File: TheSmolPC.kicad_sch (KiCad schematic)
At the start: 0 parts

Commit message: partially finished the schematic ig
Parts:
- added C1, C12, C2: 0.1u, Capacitor_SMD:C_0402_1005Metric, symbol Device:C
- added C10, C11, C16, C17, C18, C19, C20, C21, C22, C23, C24, C8, C9: 100n, Capacitor_SMD:C_0402_1005Metric, symbol Device:C
- added C13, C14, C15: 10u, Capacitor_SMD:C_0402_1005Metric, symbol Device:C
- added C3, C4: 34pF, Capacitor_SMD:C_0402_1005Metric, symbol Device:C
- added C5, C6, C7: 4.7u, Capacitor_SMD:C_0402_1005Metric, symbol Device:C
- added D1: MBR120VLSFT1G, Diode_SMD:D_SOD-123F, symbol Device:D_Schottky
- added J1: USB_C_Receptacle_USB2.0_16P, Connector_USB:USB_C_Receptacle_GCT_USB4105-xx-A_16P_TopMnt_Horizontal, symbol Connector:USB_C_Receptacle_USB2.0_16P
- added J2, J3: USB_A, Connector_USB:USB_A_Receptacle_GCT_USB1046, symbol Connector:USB_A
- added J4: HDMI_A, Connector_Video:HDMI_A_Molex_208658-1001_Horizontal, symbol Connector:HDMI_A
- added L1: 2.2u, Inductor_SMD:L_Changjiang_FNR3015S, symbol Device:L
- added L2: 3.3u, Inductor_SMD:L_Murata_DFE201610P, symbol Device:L
- added R1, R2: 5.1k, Resistor_SMD:R_0402_1005Metric, symbol Device:R
- added R3, R4: 27, Resistor_SMD:R_0402_1005Metric, symbol Device:R
- added R5: 100, Resistor_SMD:R_0402_1005Metric, symbol Device:R
- added R5: 560k, Resistor_SMD:R_0402_1005Metric, symbol Device:R
- added R6: 100k, Resistor_SMD:R_0402_1005Metric, symbol Device:R
- added R7: 33, Resistor_SMD:R_0402_1005Metric, symbol Device:R
- added R8: 10k, Resistor_SMD:R_0402_1005Metric, symbol Device:R
- added RN1, RN2, RN3, RN4: 220, Resistor_SMD:R_Array_Convex_2x0402, symbol Device:R_Pack02
- added U1: RP2350B-QFN80, Package_DFN_QFN:QFN-80-1EP_10x10mm_P0.4mm_EP3.4x3.4mm_ThermalVias, symbol rp2350b-qfn80:RP2350B-QFN80
- added U2: CH334R, Package_QFP:HTQFP-64-1EP_10x10mm_P0.5mm_EP8x8mm_Mask4.4x4.4mm_ThermalVias, symbol Interface_USB:CH334R
- added U3: TPS63000, Package_SON:Texas_DRC0010J_ThermalVias, symbol Regulator_Switching:TPS63000
- added U4: W25Q128JVS, Package_SO:SOIC-8_5.3x5.3mm_P1.27mm, symbol Memory_Flash:W25Q128JVS
- added U5: APS6404L-SQRx-SN, Package_SO:SOIC-8_3.9x4.9mm_P1.27mm, symbol Memory_RAM:APS6404L-SQRx-SN
- added Y1: 12MHz, Crystal:Crystal_SMD_Abracon_ABM3-2Pin_5.0x3.2mm, symbol Device:Crystal_Small
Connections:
- new net: C4.1, U2.15 (XO), Y1.1
- new net: C3.1, U2.16 (XI), Y1.2
- new net: C7.1, R7.2, U1.61 (VREG_AVDD)
- new net: R4.1, U1.66 (USB_DM)
- new net: R3.1, U1.67 (USB_DP)
- new net: C12.1, R5.2, U3.6 (EN), U3.7 (PS/SYNC), U3.8 (VINA)
- new net: R5.2, R6.1, U3.10 (FB)
- new net: L1.1, U3.2 (L2)
- new net: L1.2, U3.4 (L1)
- new net: J1.A5 (CC1), R1.1
- new net: J1.B5 (CC2), R2.1
- new net +1V1: C21.1, C22.1, C23.1, C5.1, L2.1, U1.10 (DVDD), U1.32 (DVDD), U1.51 (DVDD), U1.65 (VREG_FB), U1.69 (QSPI_IOVDD)
- new net +3V3: C10.1, C11.1, C14.1, C15.1, C16.1, C17.1, C18.1, C19.1, C20.1, C24.1, C6.1, C8.1, C9.1, R5.1, R7.1, R8.1, U1.15 (IOVDD), U1.24 (IOVDD), U1.29 (IOVDD), U1.41 (IOVDD), U1.5 (IOVDD), U1.50 (IOVDD), U1.59 (ADC_AVDD), U1.60 (IOVDD), U1.64 (VREG_VIN), U1.68 (USB_OTP_VDD), U1.76 (IOVDD), U3.1 (VOUT), U4.8 (VCC)
- new net +3V3_USB: C1.1, U2.13 (VDD33)
- new net DVI_CK+: J4.10 (CK+), RN4.4 (R1.2)
- new net DVI_CK-: J4.12 (CK-), RN4.3 (R2.2)
- new net DVI_D0+: J4.7 (D0+), RN3.4 (R1.2)
- new net DVI_D0-: J4.9 (D0-), RN3.3 (R2.2)
- new net DVI_D1+: J4.4 (D1+), RN2.4 (R1.2)
- new net DVI_D1-: J4.6 (D1-), RN2.3 (R2.2)
- new net DVI_D2+: J4.1 (D2+), RN1.4 (R1.2)
- new net DVI_D2-: J4.3 (D2-), RN1.3 (R2.2)
- new net FLASH_CLK: U1.71 (QSPI_SCLK), U4.6 (CLK), U5.6 (SCLK)
- new net FLASH_CS: R8.2, U1.75 (QSPI_SS), U4.1 (~{CS})
- new net FLASH_SD0: U1.72 (QSPI_SD0), U4.5 (DI/IO_{0}), U5.5 (SI/SIO0)
- new net FLASH_SD1: U1.74 (QSPI_SD1), U4.2 (DO/IO_{1}), U5.2 (SO/SIO1)
- new net FLASH_SD2: U1.73 (QSPI_SD2), U4.3 (~{WP}/IO_{2}), U5.3 (SIO2)
- new net FLASH_SD3: U1.70 (QSPI_SD3), U4.7 (~{HOLD}/~{RESET}/IO_{3}), U5.7 (SIO3)
- new net GND: C1.2, C10.2, C11.2, C12.2, C13.2, C14.2, C15.2, C16.2, C17.2, C18.2, C19.2, C2.2, C20.2, C21.2, C22.2, C23.2, C24.2, C3.2, C4.2, C5.2, C6.2, C7.2, C8.2, C9.2, J1.A1 (GND), J1.A12 (GND), J1.B1 (GND), J1.B12 (GND), J1.S1 (SHIELD), J2.4 (GND), J2.5 (Shield), J3.4 (GND), J3.5 (Shield), R1.2, R2.2, R6.2, U1.62 (VREG_PGND), U2.14 (GND), U3.11 (PGND), U3.3 (PGND), U3.9 (GND), U4.4 (GND)
- new net HSTX_CK+: RN4.1 (R1.1), U1.11 (GPIO12)
- new net HSTX_CK-: RN4.2 (R2.1), U1.12 (GPIO13)
- new net HSTX_D0+: RN3.1 (R1.1), U1.13 (GPIO14)
- new net HSTX_D0-: RN3.2 (R2.1), U1.14 (GPIO15)
- new net HSTX_D1+: RN2.1 (R1.1), U1.16 (GPIO16)
- new net HSTX_D1-: RN2.2 (R2.1), U1.17 (GPIO17)
- new net HSTX_D2+: RN1.1 (R1.1), U1.18 (GPIO18)
- new net HSTX_D2-: RN1.2 (R2.1), U1.19 (GPIO19)
- new net USB0_D+: J2.3 (D+), U2.8 (DP1+)
- new net USB0_D-: J2.2 (D-), U2.7 (DM1-)
- new net USB1_D+: J3.3 (D+), U2.6 (DP2+)
- new net USB1_D-: J3.2 (D-), U2.5 (DM2-)
- new net USB_D+: J1.A6 (D+), J1.B6 (D+), R3.2, U2.11 (DPU+)
- new net USB_D-: J1.A7 (D-), J1.B7 (D-), R4.2, U2.10 (DMU-)
- new net VBUS: D1.2 (A), J1.A4 (VBUS), J1.A9 (VBUS), J1.B4 (VBUS), J1.B9 (VBUS), J2.1 (VBUS), J3.1 (VBUS)
- new net VREG_LX: L2.2, U1.63 (VREG_LX)
- new net VSYS: C13.1, C2.1, D1.1 (K), R5.1, U2.12 (V5), U3.5 (VIN)
- no-connect marks 0 -> 8
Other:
- note added: "I'll probably use this USB line as usages for USB by the host PC or the RP2350"
- note added: "who needs CEC anw"

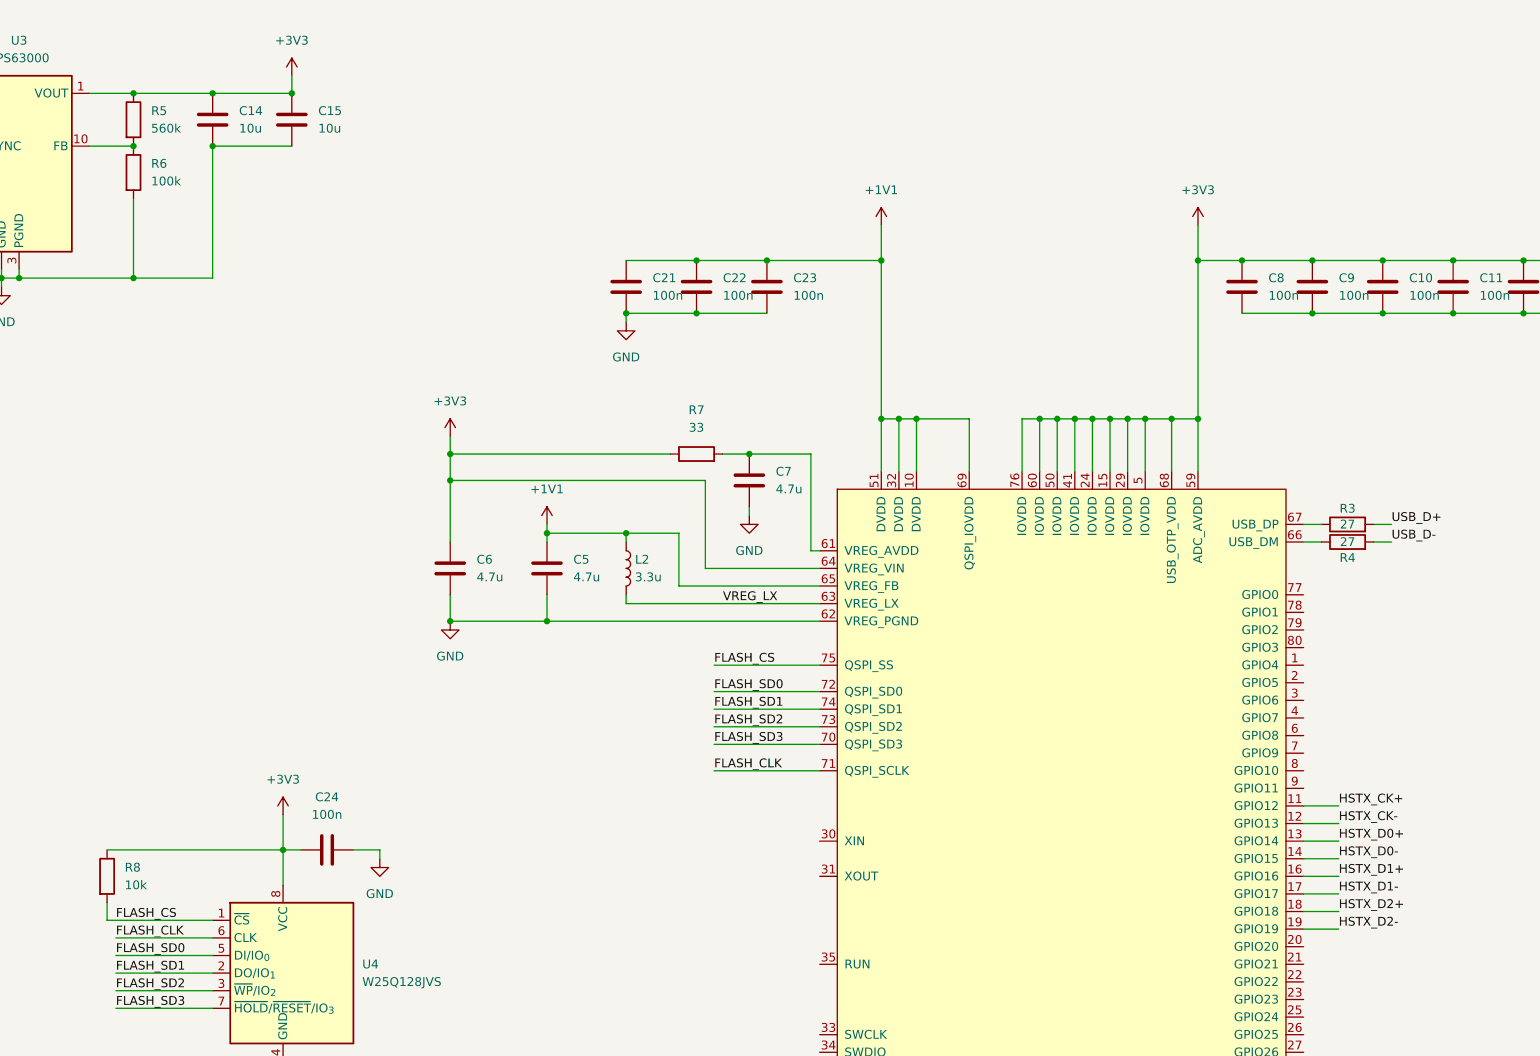
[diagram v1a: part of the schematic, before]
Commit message: fixed the schematic differential pair polarities (tested with the pcb editor)
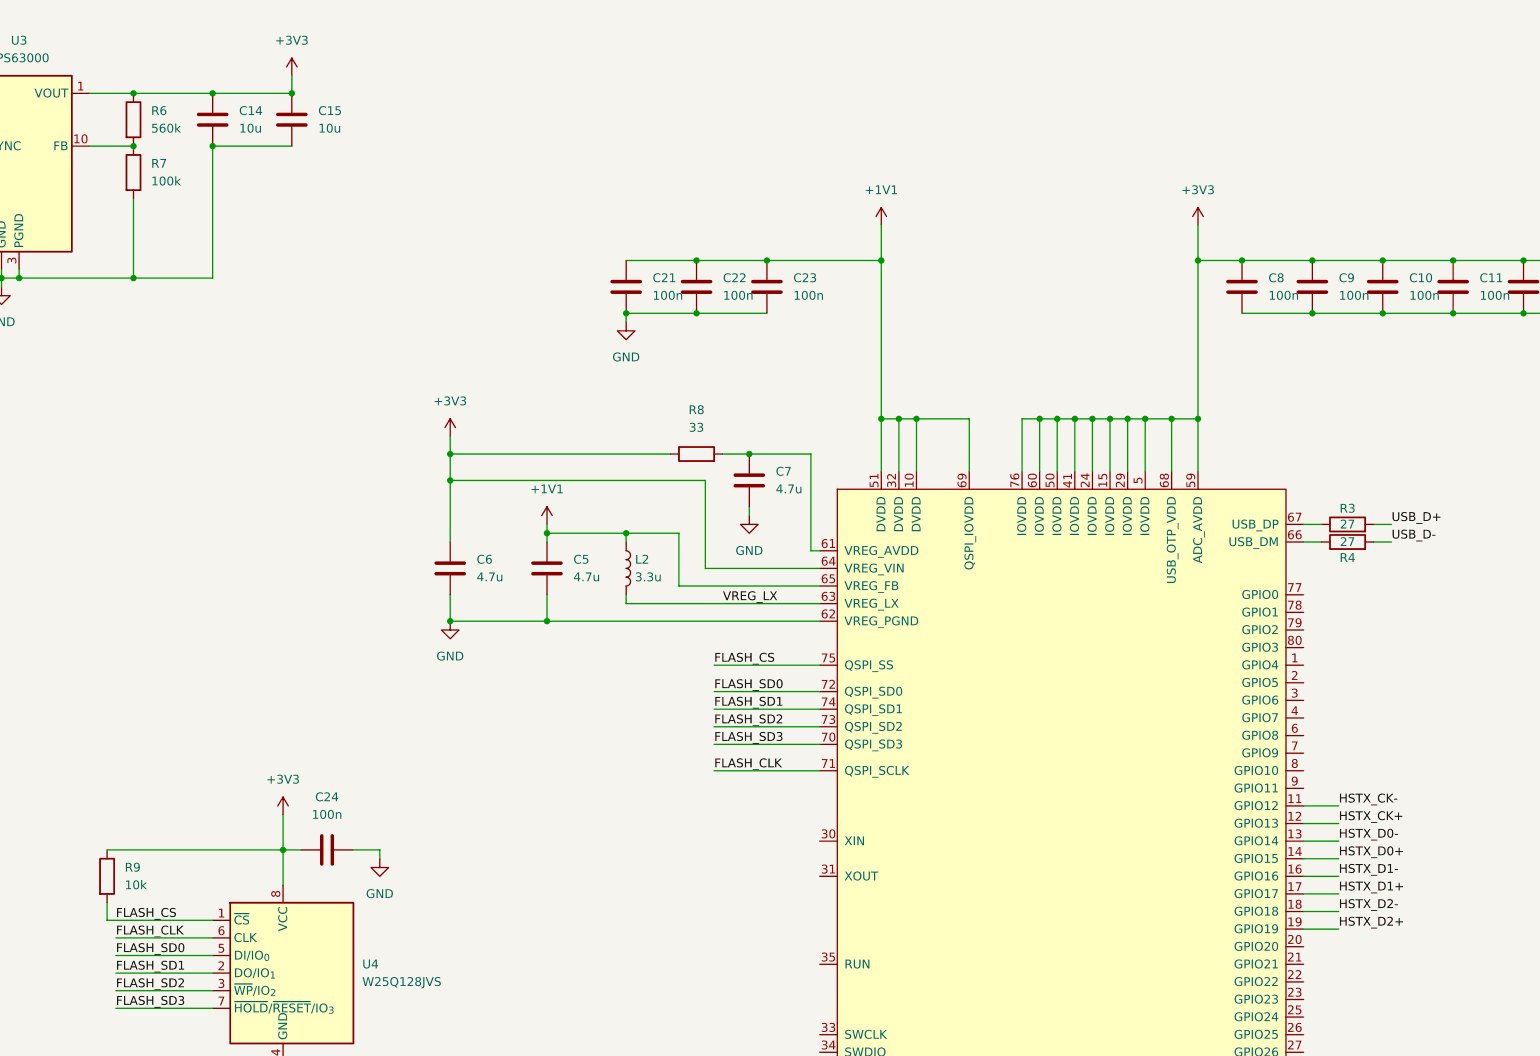
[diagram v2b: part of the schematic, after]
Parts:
- U2: footprint Package_QFP:HTQFP-64-1EP_10x10mm_P0.5mm_EP8x8mm_Mask4.4x4.4mm_ThermalVias -> Package_SO:QSOP-16_3.9x4.9mm_P0.635mm
- renumbered R5 to R6, R6 to R7, R7 to R8, R8 to R9
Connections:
- net HSTX_CK+: now also U1.12 (GPIO13); no longer U1.11 (GPIO12)
- net HSTX_CK-: now also U1.11 (GPIO12); no longer U1.12 (GPIO13)
- net HSTX_D0+: now also U1.14 (GPIO15); no longer U1.13 (GPIO14)
- net HSTX_D0-: now also U1.13 (GPIO14); no longer U1.14 (GPIO15)
- net HSTX_D1+: now also U1.17 (GPIO17); no longer U1.16 (GPIO16)
- net HSTX_D1-: now also U1.16 (GPIO16); no longer U1.17 (GPIO17)
- net HSTX_D2+: now also U1.19 (GPIO19); no longer U1.18 (GPIO18)
- net HSTX_D2-: now also U1.18 (GPIO18); no longer U1.19 (GPIO19)
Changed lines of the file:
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@@
 	(wire
 		(pts
-			(xy 322.58 132.08) (xy 317.5 132.08)
-		)
-		(stroke
-			(width 0)
-			(type default)
-		)
-	)
-	(wire
-		(pts
 			(xy 146.05 153.67) (xy 160.02 153.67)
 		)
@@
 	(wire
 		(pts
-			(xy 322.58 129.54) (xy 317.5 129.54)
-		)
-		(stroke
-			(width 0)
-			(type default)
-		)
-	)
-	(wire
-		(pts
 			(xy 45.72 113.03) (xy 35.56 113.03)
 		)
@@
 	(wire
 		(pts
-			(xy 82.55 111.76) (xy 69.85 111.76)
+			(xy 322.58 142.24) (xy 317.5 142.24)
 		)
 		(stroke
@@
 	(wire
 		(pts
-			(xy 146.05 158.75) (xy 160.02 158.75)
+			(xy 317.5 129.54) (xy 322.58 129.54)
 		)
 		(stroke
@@
 	(wire
 		(pts
-			(xy 302.26 73.66) (xy 302.26 81.28)
+			(xy 82.55 111.76) (xy 69.85 111.76)
 		)
 		(stroke
@@
 	(wire
 		(pts
-			(xy 292.1 73.66) (xy 294.64 73.66)
+			(xy 146.05 158.75) (xy 160.02 158.75)
 		)
 		(stroke
@@
 	(wire
 		(pts
-			(xy 322.58 142.24) (xy 317.5 142.24)
+			(xy 302.26 73.66) (xy 302.26 81.28)
+		)
+		(stroke
+			(width 0)
+			(type default)
+		)
+	)
+	(wire
+		(pts
+			(xy 292.1 73.66) (xy 294.64 73.66)
 		)
 		(stroke
@@
 	(wire
 		(pts
-			(xy 322.58 139.7) (xy 317.5 139.7)
+			(xy 232.41 118.11) (xy 247.65 118.11)
 		)
 		(stroke
@@
 	(wire
 		(pts
-			(xy 232.41 118.11) (xy 247.65 118.11)
+			(xy 322.58 144.78) (xy 317.5 144.78)
 		)
 		(stroke
@@
 	(wire
 		(pts
-			(xy 322.58 134.62) (xy 317.5 134.62)
-		)
-		(stroke
-			(width 0)
-			(type default)
-		)
-	)
-	(wire
-		(pts
 			(xy 287.02 73.66) (xy 287.02 81.28)
 		)
@@
 	(wire
 		(pts
+			(xy 322.58 134.62) (xy 317.5 134.62)
+		)
+		(stroke
+			(width 0)
+			(type default)
+		)
+	)
+	(wire
+		(pts
 			(xy 59.69 67.31) (xy 59.69 81.28)
 		)
@@
 	(wire
 		(pts
+			(xy 322.58 147.32) (xy 317.5 147.32)
+		)
+		(stroke
+			(width 0)
+			(type default)
+		)
+	)
+	(wire
+		(pts
 			(xy 289.56 73.66) (xy 292.1 73.66)
 		)
@@
 	(wire
 		(pts
+			(xy 322.58 139.7) (xy 317.5 139.7)
+		)
+		(stroke
+			(width 0)
+			(type default)
+		)
+	)
+	(wire
+		(pts
 			(xy 208.28 102.87) (xy 247.65 102.87)
 		)
@@
 	(wire
 		(pts
+			(xy 322.58 132.08) (xy 317.5 132.08)
+		)
+		(stroke
+			(width 0)
+			(type default)
+		)
+	)
+	(wire
+		(pts
 			(xy 85.09 92.71) (xy 85.09 102.87)
 		)
@@
 	(wire
 		(pts
-			(xy 322.58 147.32) (xy 317.5 147.32)
-		)
-		(stroke
-			(width 0)
-			(type default)
-		)
-	)
-	(wire
-		(pts
 			(xy 107.95 53.34) (xy 99.06 53.34)
 		)
@@
 	(wire
 		(pts
-			(xy 322.58 144.78) (xy 317.5 144.78)
+			(xy 322.58 137.16) (xy 317.5 137.16)
 		)
 		(stroke
@@
 	(wire
 		(pts
-			(xy 322.58 137.16) (xy 317.5 137.16)
-		)
-		(stroke
-			(width 0)
-			(type default)
-		)
-	)
-	(wire
-		(pts
 			(xy 294.64 73.66) (xy 298.45 73.66)
 		)
@@
 	)
 	(label "HSTX_D0+"
-		(at 322.58 134.62 0)
+		(at 322.58 137.16 0)
 		(effects
 			(font
@@
 	)
 	(label "HSTX_D2-"
-		(at 322.58 147.32 0)
+		(at 322.58 144.78 0)
 		(effects
 			(font
@@
 	)
 	(label "HSTX_D1+"
-		(at 322.58 139.7 0)
+		(at 322.58 142.24 0)
 		(effects
 			(font
@@
 	)
 	(label "HSTX_CK+"
-		(at 322.58 129.54 0)
+		(at 322.58 132.08 0)
 		(effects
 			(font
@@
 	)
 	(label "HSTX_D1-"
-		(at 322.58 142.24 0)
+		(at 322.58 139.7 0)
 		(effects
 			(font
@@
 	)
 	(label "HSTX_D0-"
-		(at 322.58 137.16 0)
+		(at 322.58 134.62 0)
 		(effects
 			(font
@@
 	)
 	(label "HSTX_D2+"
-		(at 322.58 144.78 0)
+		(at 322.58 147.32 0)
 		(effects
 			(font
@@
 	)
 	(label "HSTX_CK-"
-		(at 322.58 132.08 0)
+		(at 322.58 129.54 0)
 		(effects
 			(font
@@
 		(dnp no)
 		(fields_autoplaced yes)
-		(property "Reference" "R8"
+		(property "Reference" "R9"
 			(at 147.32 138.4299 0)
 			(effects
@@
 			(project ""
 				(path "/4f27cb06-5d2e-405b-b263-d7303bcdacf8"
-					(reference "R8")
+					(reference "R9")
 					(unit 1)
 				)
@@
 			)
 		)
-		(property "Footprint" "Package_QFP:HTQFP-64-1EP_10x10mm_P0.5mm_EP8x8mm_Mask4.4x4.4mm_ThermalVias"
+		(property "Footprint" "Package_SO:QSOP-16_3.9x4.9mm_P0.635mm"
 			(at 62.23 124.46 0)
 			(effects
@@
 		(dnp no)
 		(fields_autoplaced yes)
-		(property "Reference" "R7"
+		(property "Reference" "R8"
 			(at 229.87 72.39 90)
 			(effects
@@
 			(project ""
 				(path "/4f27cb06-5d2e-405b-b263-d7303bcdacf8"
-					(reference "R7")
+					(reference "R8")
 					(unit 1)
 				)
@@
 		(dnp no)
 		(fields_autoplaced yes)
-		(property "Reference" "R6"
+		(property "Reference" "R7"
 			(at 151.13 36.8299 0)
 			(effects
@@
 			(project "TheSmolPC"
 				(path "/4f27cb06-5d2e-405b-b263-d7303bcdacf8"
-					(reference "R6")
+					(reference "R7")
 					(unit 1)
 				)
@@
 		(dnp no)
 		(fields_autoplaced yes)
-		(property "Reference" "R5"
+		(property "Reference" "R6"
 			(at 151.13 29.2099 0)
 			(effects
@@
 			(project "TheSmolPC"
 				(path "/4f27cb06-5d2e-405b-b263-d7303bcdacf8"
-					(reference "R5")
+					(reference "R6")
 					(unit 1)
 				)

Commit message: recompleting the schema so now its full
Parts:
- added C25, C26: 15p, Capacitor_SMD:C_0402_1005Metric, symbol Device:C
- added C27, C28, C30, C32: 100n, Capacitor_SMD:C_0402_1005Metric, symbol Device:C
- added C29, C31, C33, C35: 10u, Capacitor_SMD:C_0402_1005Metric, symbol Device:C
- added C34, C36: 2.2u, Capacitor_SMD:C_0402_1005Metric, symbol Device:C
- added J5: Micro_SD_Card_Det2, Connector_Card:microSD_HC_Hirose_DM3D-SF, symbol Connector:Micro_SD_Card_Det2
- added J6: Conn_01x04, Connector_JST:JST_SH_SM04B-SRSS-TB_1x04-1MP_P1.00mm_Horizontal, symbol Connector_Generic:Conn_01x04
- added J7: Conn_01x03, Connector_JST:JST_SH_SM03B-SRSS-TB_1x03-1MP_P1.00mm_Horizontal, symbol Connector_Generic:Conn_01x03
- added J8: AudioJack4_Ground, Connector_Audio:Jack_3.5mm_CUI_SJ1-3515N_Horizontal, symbol Connector_Audio:AudioJack4_Ground
- added R10: 1k, Resistor_SMD:R_0402_1005Metric, symbol Device:R
- added R11, R14, R15, R16: 10k, Resistor_SMD:R_0402_1005Metric, symbol Device:R
- added R12, R13: 100k, Resistor_SMD:R_0402_1005Metric, symbol Device:R
- added SW1: SW_Push, Button_Switch_SMD:SW_Push_1P1T_NO_Vertical_Wuerth_434133025816, symbol Switch:SW_Push
- added TP1: BOOT, TestPoint:TestPoint_Pad_D1.0mm, symbol Connector:TestPoint
- added U6: TXS0102DQE, Package_SON:X2SON-8_1.4x1mm_P0.35mm, symbol Logic_LevelTranslator:TXS0102DQE
- added U7: ESP32-C6-MINI-1, RF_Module:ESP32-C6-MINI-1, symbol RF_Module:ESP32-C6-MINI-1
- added U8: PCM5101A, Package_SO:TSSOP-20_4.4x6.5mm_P0.65mm, symbol Audio:PCM5101A
- added Y2: 12MHz, Crystal:Crystal_SMD_3225-4Pin_3.2x2.5mm, symbol Device:Crystal_GND24
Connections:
- net +3V3: now also U5.8 (VDD), C27.1, C32.1, C33.1, J5.4 (VDD), J6.2 (Pin_2), R11.1, R14.1, R15.1, R16.1, U6.1 (VCCA), U6.5 (OE), U7.22 (IO8), U7.3 (3V3), U8.17 (XSMT), U8.20 (DVDD)
- net FLASH_CS: now also SW1.2
- net GND: now also J4.11 (CKS), J4.17 (GND), J4.2 (D2S), J4.5 (D1S), J4.8 (D0S), J4.SH, U1.81 (GND), U5.4 (VSS), C25.2, C26.2, C27.2, C28.2, C29.2, C30.2, C31.2, C32.2, C33.2, C34.2, C35.2, J5.11 (SHIELD), J5.6 (VSS), J6.1 (Pin_1), J7.2 (Pin_2), J8.G, J8.R2, R13.1, SW1.1, U6.4 (GND), U7.1 (GND), U7.11 (GND), U7.14 (GND), U7.2 (GND), U7.36 (GND), U7.37 (GND), U7.38 (GND), U7.39 (GND), U7.40 (GND), U7.41 (GND), U7.42 (GND), U7.43 (GND), U7.44 (GND), U7.45 (GND), U7.46 (GND), U7.47 (GND), U7.48 (GND), U7.49 (GND), U7.50 (GND), U7.51 (GND), U7.52 (GND), U7.53 (GND), U7.6 (IO3), U8.10 (DEMP), U8.11 (FLT), U8.12 (SCK), U8.16 (FMT), U8.19 (DGND), U8.3 (CPGND), U8.9 (AGND), Y2.2, Y2.4
- net VSYS: now also J4.18 (+5V), U6.8 (VCCB)
- net HSTX_SDA: now reaches U1.20 (GPIO20)
- net HSTX_SDA: now also U6.3 (A2)
- net HSTX_SCL: now reaches U1.21 (GPIO21)
- net HSTX_SCL: now also U6.2 (A1)
- net HDMI_HPD: now reaches U1.22 (GPIO22)
- net HDMI_HPD: now also R12.1, R13.2
- net ESP_RST: now reaches U1.23 (GPIO23)
- net ESP_RST: now also R15.2, U7.8 (EN)
- net at U1.30 (XIN): now also C26.1, Y2.1
- net at U1.31 (XOUT): now also R10.2
- net DBG_CLK: now reaches U1.33 (SWCLK)
- net DBG_CLK: now also J7.1 (Pin_1)
- net DBG_DIO: now reaches U1.34 (SWDIO)
- net DBG_DIO: now also J7.3 (Pin_3)
- net SDIO_DET: now reaches U1.42 (GPIO33)
- net SDIO_DET: now also J5.10 (DET_A)
- net SDIO_CLK: now reaches U1.43 (GPIO34)
- net SDIO_CLK: now also J5.5 (CLK)
- net SDIO_CMD: now reaches U1.44 (GPIO35)
- net SDIO_CMD: now also J5.3 (CMD)
- net SDIO_D0: now reaches U1.45 (GPIO36)
- net SDIO_D0: now also J5.7 (DAT0)
- net SDIO_D1: now reaches U1.46 (GPIO37)
- net SDIO_D1: now also J5.8 (DAT1)
- net SDIO_D2: now reaches U1.47 (GPIO38)
- net SDIO_D2: now also J5.1 (DAT2)
- net SDIO_D3: now reaches U1.48 (GPIO39)
- net SDIO_D3: now also J5.2 (DAT3/CD), R14.2
- net PCM_LRCLK: now reaches U1.55 (GPIO44_ADC4)
- net PCM_LRCLK: now also U8.15 (LRCK)
- net PCM_DIN: now reaches U1.56 (GPIO45_ADC5)
- net PCM_DIN: now also U8.14 (DIN)
- net PCB_BCK: now reaches U1.57 (GPIO46_ADC6)
- net PCB_BCK: now also U8.13 (BCK)
- net PSRAM_CS: now reaches U1.58 (GPIO47_ADC7)
- net PSRAM_CS: now also U5.1 (~{CE}), R11.2
- net ESP_RX_TO_TX: now reaches U1.6 (GPIO8)
- net ESP_RX_TO_TX: now also U7.30 (RXD0)
- net ESP_TX_TO_RX: now reaches U1.7 (GPIO9)
- net ESP_TX_TO_RX: now also U7.31 (TXD0)
- net GEN_SDA: now reaches U1.79 (GPIO2)
- net GEN_SDA: now also J6.3 (Pin_3)
- net GEN_SCL: now reaches U1.80 (GPIO3)
- net GEN_SCL: now also J6.4 (Pin_4)
- net at J4.15 (SCL): now also U6.7 (B1)
- net at J4.16 (SDA): now also U6.6 (B2)
- net at J4.19 (HPD): now also R12.2
- new net: C36.1, U8.2 (CAPP)
- new net: C36.2, U8.4 (CAPM)
- new net: C35.1, U8.18 (LDOO)
- new net: C34.1, U8.5 (VNEG)
- new net: C25.1, R10.1, Y2.3
- new net: R16.2, TP1.1, U7.23 (IO9)
- new net +3.3VA: C28.1, C29.1, C30.1, C31.1, U8.1 (CPVDD), U8.8 (AVDD)
- new net AUX_OUTL: J8.R1, U8.6 (OUTL)
- new net AUX_OUTR: J8.T, U8.7 (OUTR)
- new net ESP_BZ: U7.24 (IO18)
- new net ESP_CLK: U7.28 (IO22)
- new net ESP_CS: U7.16 (IO7)
- new net ESP_MISO: U7.15 (IO6)
- new net ESP_MOSI: U7.27 (IO21)
- no-connect marks 8 -> 23
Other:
- moved on the sheet: C24, J4, R9, U4, U5
